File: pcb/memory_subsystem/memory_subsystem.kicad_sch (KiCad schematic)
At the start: 29 parts, among them J1 CLK, J2 Addr In, J3 Data In, J4 Word In, J5 Power, SW1 RUN, SW2 HLT, SW3 HLT Word, SW4 SW_DIP_x01

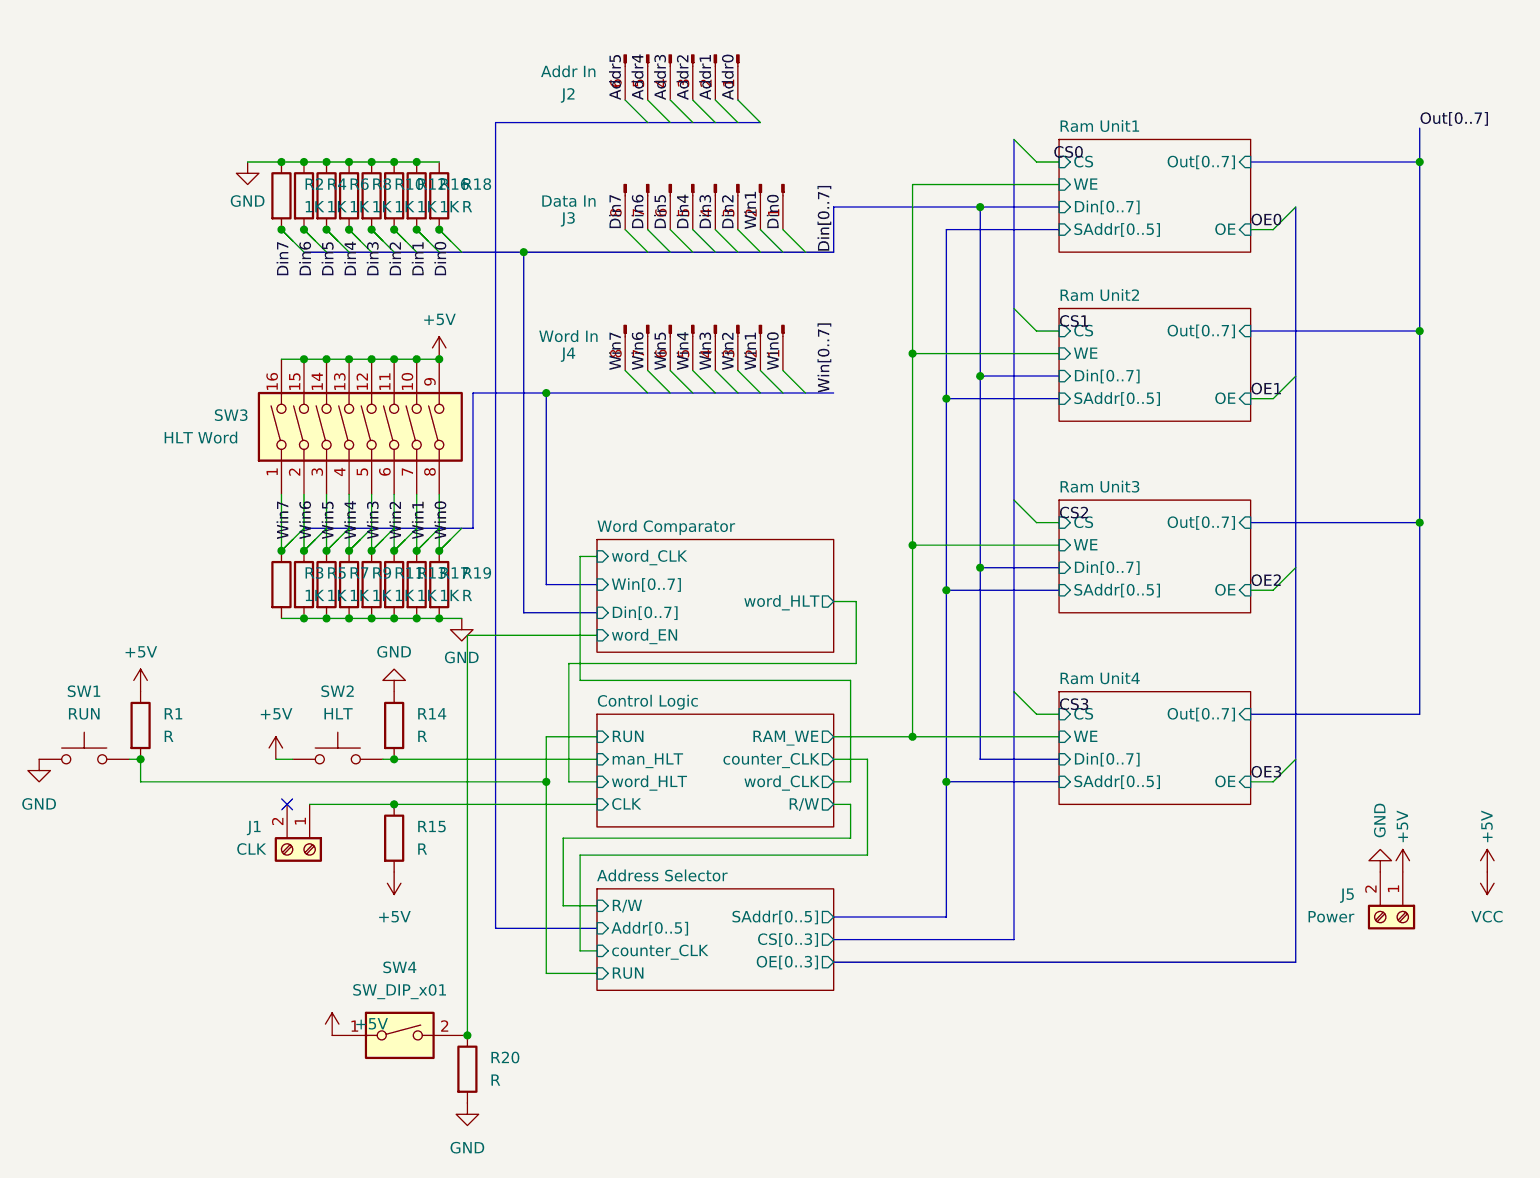
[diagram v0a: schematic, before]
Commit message: Fixed spacing problem: no warnings/erros
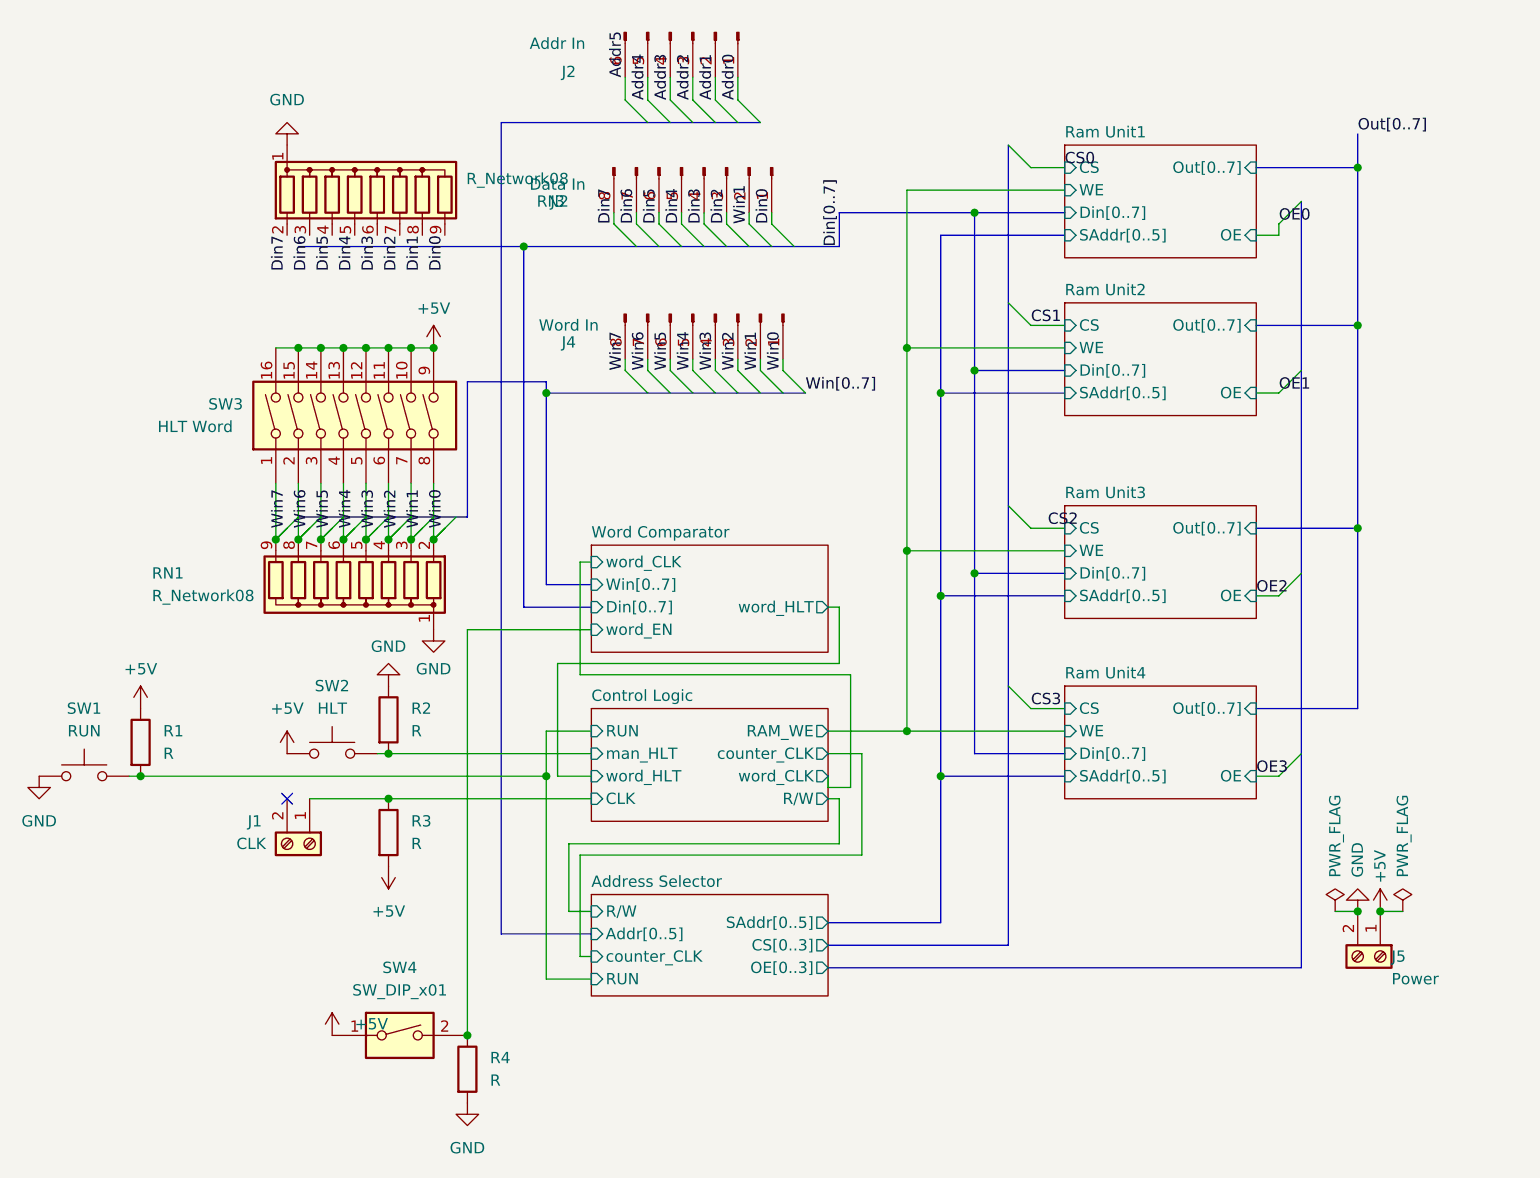
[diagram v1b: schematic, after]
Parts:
- removed R10, R11, R12, R13, R16, R17, R2, R3, R4, R5, R6, R7, R8, R9: 1K, symbol Device:R
- removed R18, R19: R, symbol Device:R
- added RN1, RN2: R_Network08, Resistor_THT:R_Array_SIP9, symbol Device:R_Network08
- renumbered R14 to R2, R15 to R3, R20 to R4
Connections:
- net Din0: now also RN2.9 (R8)
- net Din1: now also RN2.8 (R7)
- net Din2: now also RN2.7 (R6)
- net Din3: now also RN2.6 (R5)
- net Din4: now also RN2.5 (R4)
- net Din5: now also RN2.4 (R3)
- net Din6: now also RN2.3 (R2)
- net Din7: now also RN2.2 (R1)
- net GND: now also RN1.1 (common), RN2.1 (common)
- net Win0: now also RN1.2 (R1)
- net Win1: now also RN1.3 (R2)
- net Win2: now also RN1.4 (R3)
- net Win3: now also RN1.5 (R4)
- net Win4: now also RN1.6 (R5)
- net Win5: now also RN1.7 (R6)
- net Win6: now also RN1.8 (R7)
- net Win7: now also RN1.9 (R8)
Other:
- moved on the sheet: J1, J2, J3, J4, J5, R1, R2, R3, SW1, SW2, SW3

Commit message: Tracks finished
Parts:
- removed J4: Word In, symbol Connector:Conn_01x08_Pin
- removed RN1, RN2: R_Network08, Resistor_THT:R_Array_SIP9, symbol Device:R_Network08
- added J6: Data Out, Connector_PinHeader_2.54mm:PinHeader_1x08_P2.54mm_Vertical, symbol Connector:Conn_01x08_Pin
- added R10, R11, R12, R13, R14, R15, R16, R17, R18, R19, R20, R5, R6, R7, R8, R9: R, Resistor_SMD:R_0805_2012Metric_Pad1.20x1.40mm_HandSolder, symbol Device:R
- J1, J5: footprint (none) -> TerminalBlock_Phoenix:TerminalBlock_Phoenix_MKDS-1,5-2_1x02_P5.00mm_Horizontal
- J2: footprint (none) -> Connector_PinHeader_2.54mm:PinHeader_1x06_P2.54mm_Vertical
- J3: footprint (none) -> Connector_PinHeader_2.54mm:PinHeader_1x08_P2.54mm_Vertical
- R1, R2, R3, R4: footprint (none) -> Resistor_SMD:R_0805_2012Metric_Pad1.20x1.40mm_HandSolder
- SW1, SW2: footprint (none) -> Button_Switch_THT:SW_TH_Tactile_Omron_B3F-100x
- SW3: footprint (none) -> Button_Switch_THT:SW_DIP_SPSTx08_Slide_9.78x22.5mm_W7.62mm_P2.54mm
- SW4: value SW_DIP_x01 -> W_EN; footprint (none) -> Button_Switch_THT:SW_DIP_SPSTx01_Slide_9.78x4.72mm_W7.62mm_P2.54mm
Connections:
- net Din0: now also R5.1
- net Din1: now also J3.2 (Pin_2), R6.1
- net Din2: now also R7.1
- net Din3: now also R8.1
- net Din4: now also R9.1
- net Din5: now also R10.1
- net Din6: now also R11.1
- net Din7: now also R12.1
- net GND: now also R10.2, R11.2, R12.2, R13.2, R14.2, R15.2, R16.2, R17.2, R18.2, R19.2, R20.2, R5.2, R6.2, R7.2, R8.2, R9.2
- net Win0: now also R13.1
- net Win1: now also R14.1; no longer J3.2 (Pin_2)
- net Win2: now also R15.1
- net Win3: now also R16.1
- net Win4: now also R17.1
- net Win5: now also R18.1
- net Win6: now also R19.1
- net Win7: now also R20.1
- new net Out0: J6.8 (Pin_8)
- new net Out1: J6.7 (Pin_7)
- new net Out2: J6.6 (Pin_6)
- new net Out3: J6.5 (Pin_5)
- new net Out4: J6.4 (Pin_4)
- new net Out5: J6.3 (Pin_3)
- new net Out6: J6.2 (Pin_2)
- new net Out7: J6.1 (Pin_1)
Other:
- moved on the sheet: J1, J2, J3, J5, R1, R2, R3, R4, SW1, SW2, SW3, SW4
